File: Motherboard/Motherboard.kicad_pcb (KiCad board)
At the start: 4 copper layers, 150 x 85 mm, 340 parts, among them J1 BM09B-NSHSS-TBT_LF__SN_, J15 Bus_M.2_Socket_M, J16 Bus_M.2_Socket_E, J17 BM10B-NSHSS-TBT_LF__SN_, J19 BM04B-NSHSS-TBT_LF__SN_, J20 BM04B-NSHSS-TBT_LF__SN_, J24 200485-0710, J25 BM12B-NSHSS-TBT_LF__SN_, J4 USB3_A_Stacked, J78 Speaker_L, J79 Speaker_R, J80 USB_C_Receptacle_USB2.0_16P, J83 2004850740, J84 FFC2A33-08-T-R, J85 JST_XHP2_Battery1, J86 JST_XHP2_Battery2, J87 JST_XHP2_Battery3, J88 JST_XHP2_Battery4, J89 JST_XHP2_Battery5, J90 2004850740, J91 HDMI_A_1.4, Q11 AO3407, Q12 HM7533HBPR, Q23 AO3407, Q24 HM7533HBPR, Q25 HM7533HBPR, Q26 HM7533HBPR, Q27 HM7533HBPR, Q28 HM7533HBPR, Q29 AO3407, Q30 HM7533HBPR, Q31 HM7533HBPR, Q32 HM7533HBPR, Q78 CSD17303Q5, Q79 CSD17303Q5, Q80 2N7002, Q81 2N7002, SW78 SW_Push, SW79 SW_Push, U10 ULC0524P, U11 ULC0524P, U14 CH224K, U15 SY8253ADC, U16 SY8253ADC, U3 ULC0524P, U78 RP2040, U79 BQ25798, U80 PCM5102A, U81 TPS61088RHLR, U82 BQ27441DRZT-G1A, U83 CP2615-xx-xM, U84 PAM8403D, U85 ADS1015IDGS, U86 TPS62131, U87 STLD40DPUR, U89 D3V3XA4B10LP, U9 ULC0524P, U90 D3V3XA4B10LP, U91 D3V3XA4B10LP, U92 D3V3XA4B10LP, U95 W25Q128JVS, U96 ADV7611, U97 D3V3XA4B10LP, U98 D3V3XA4B10LP, U99 ADV7611, Y81 Crystal_GND24, Y82 Crystal_GND24

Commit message: Bottom Screen fully Wired!
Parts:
- C121, C122, C123, C124, C125, C126, C127, C90, U90: moved to B.Cu
- moved R201 17.2 mm to (120.2, 111.2)
- moved C62 14.7 mm to (95.9, 94.1)
- moved C124 8.70 mm to (168.6, 98.2)
- moved U90 7.59 mm to (169.8, 102.4), turned to -90 degrees
- moved U89 7.17 mm to (166.8, 94.9), turned to 90 degrees
- moved C121 5.13 mm to (166.6, 98.2)
- moved C123 3.60 mm to (168.1, 100.3), turned to -90 degrees
- moved C90 3.59 mm to (165.6, 98.2)
- moved C125 3.22 mm to (169.6, 98.2), turned to -90 degrees
- moved C122 1.65 mm to (167.1, 100.3), turned to -90 degrees
- moved C127 1.62 mm to (171.0, 100.3)
- moved C126 0.73 mm to (170.1, 100.3)
- moved C57 0.07 mm to (171.3, 93.5)
- moved C58 0.07 mm to (171.3, 94.5)
- moved C59 0.07 mm to (171.3, 95.5)
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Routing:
- net +5V: track 45.3 -> 109.9 mm
- net /HDMI-LVDS/DDIB_TX0+: track 0.00 -> 44.5 mm
- net /HDMI-LVDS/DDIB_TX0-: track 0.00 -> 44.5 mm
- net /HDMI-LVDS/DDIB_TX1+: track 0.00 -> 43.4 mm
- net /HDMI-LVDS/DDIB_TX1-: track 0.00 -> 43.4 mm
- net /HDMI-LVDS/DDIB_TX2+: track 0.00 -> 38.2 mm
- net /HDMI-LVDS/DDIB_TX2-: track 0.00 -> 38.2 mm
- net /HDMI-LVDS/DDIB_TX3+: track 0.00 -> 37.3 mm
- net /HDMI-LVDS/DDIB_TX3-: track 0.00 -> 37.3 mm
- net /~{PWR_LED}/~{PSON}: track 29.3 -> 10.8 mm, vias 1 -> 3
- net /HDMI-LVDS/DDIB_D2-: track 1.95 -> 14.1 mm, vias 0 -> 2
- net /HDMI-LVDS/DDIB_D2+: track 1.95 -> 14.1 mm, vias 0 -> 2
- net GND: track 153.7 -> 165.2 mm, vias 130 -> 131
- net /HDMI-LVDS/DDIB_D1-: track 3.95 -> 14.1 mm, vias 0 -> 2
- net /HDMI-LVDS/DDIB_D1+: track 3.95 -> 14.1 mm, vias 0 -> 2
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
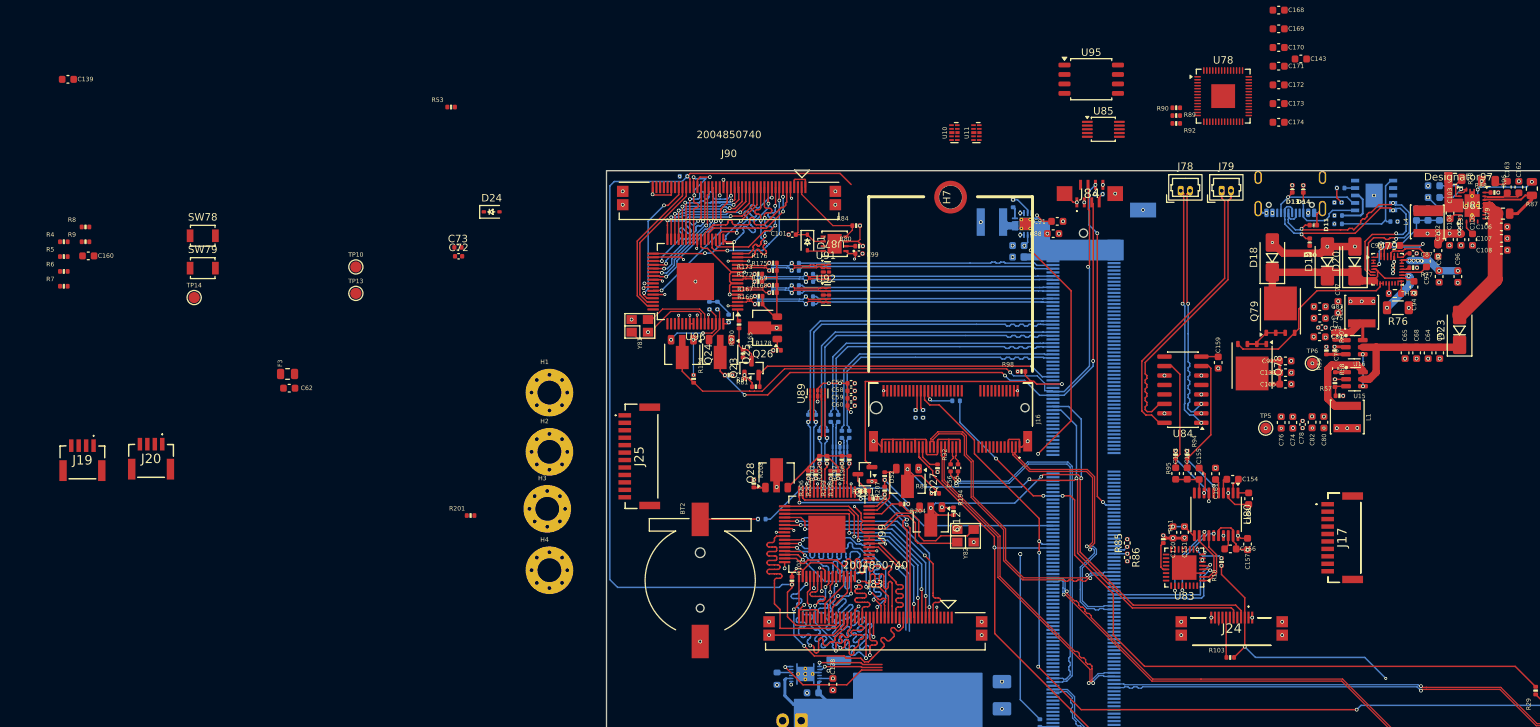
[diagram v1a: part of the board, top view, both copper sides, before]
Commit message: Corrected CTRL_PWR (+other WIP changes)
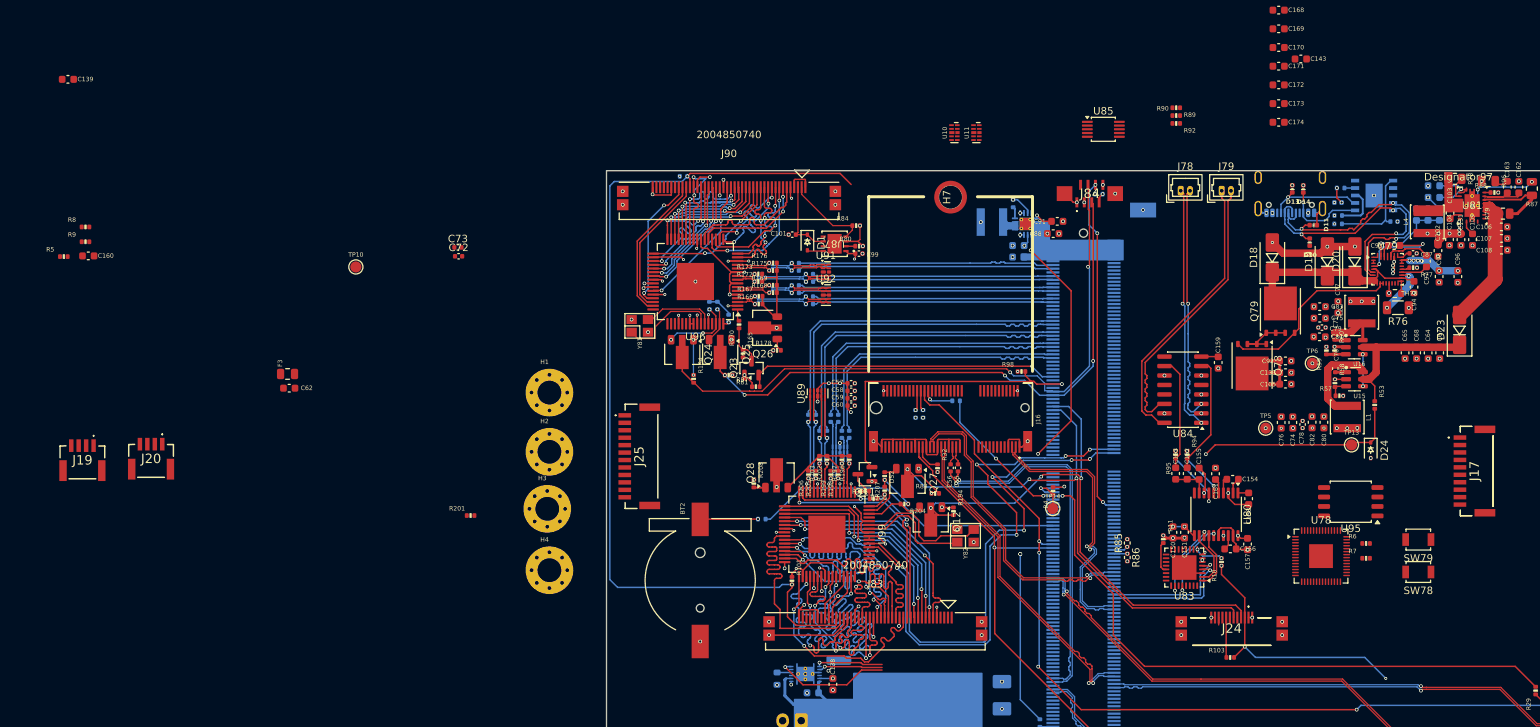
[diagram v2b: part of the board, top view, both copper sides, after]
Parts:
- moved R6 178.6 mm to (240.4, 115.0)
- moved R7 178.6 mm to (240.4, 117.0)
- moved SW78 169.3 mm to (247.5, 118.8), turned to 180 degrees
- moved SW79 167.2 mm to (247.5, 114.5), turned to 180 degrees
- moved R4 137.0 mm to (198.4, 107.9), turned to 90 degrees
- moved TP13 135.2 mm to (238.5, 101.8)
- moved R53 130.3 mm to (241.6, 96.4), turned to -90 degrees
- moved D24 122.3 mm to (241.1, 102.5), turned to -90 degrees
- moved TP14 118.7 mm to (198.4, 110.3)
- moved U95 66.6 mm to (238.4, 109.4), turned to 180 degrees
- moved U78 63.1 mm to (234.4, 116.7)
- moved J17 19.9 mm to (255.3, 105.3)
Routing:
- net /HDMI-LVDS/DDIB_ADV_SCL: track 13.9 -> 74.1 mm, vias 1 -> 5
- net /HDMI-LVDS/DDIB_ADV_SDA: track 14.8 -> 71.2 mm, vias 1 -> 5
- net VPullup: track 0.00 -> 49.9 mm, vias 0 -> 2
- net Net-(A2-~{BIOS_SEL}): track 0.00 -> 5.70 mm, vias 0 -> 1
- net VDC: track 21.5 -> 24.8 mm
- net /LattePanda Module/HSIO_3_TX+: track 49.3 -> 48.7 mm
- net /LattePanda Module/HSIO_3_TX-: track 49.3 -> 48.7 mm
- net GND: vias 131 -> 132
